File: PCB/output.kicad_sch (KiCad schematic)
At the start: 8 parts, among them J2 Output Gate, Q1 BC547

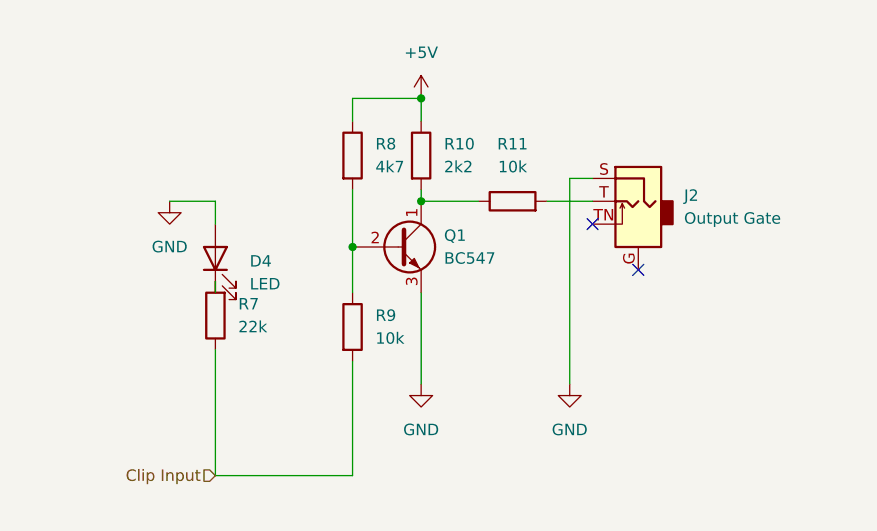
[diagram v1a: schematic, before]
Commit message: :art: Adjust layout of Clip CV input
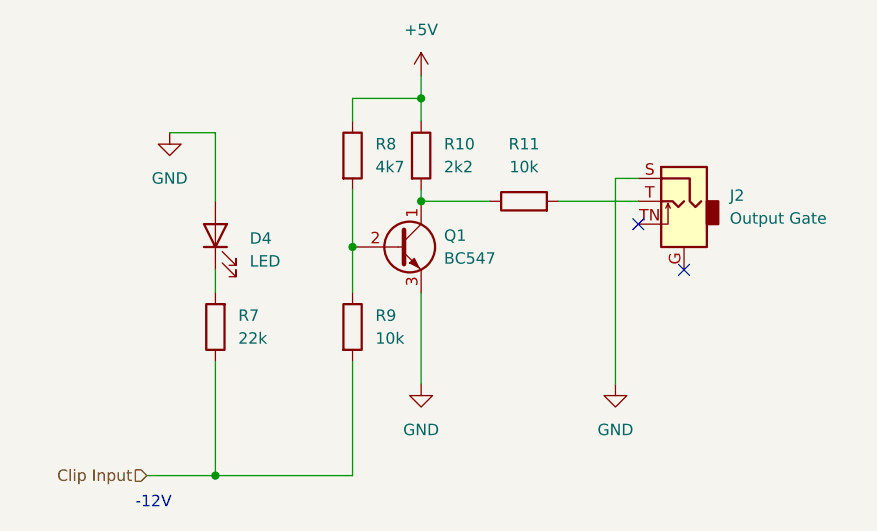
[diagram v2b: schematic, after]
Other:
- note added: "-12V"
- moved on the sheet: D4, J2, R11, R7

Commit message: :wrench: Re-assign component designators
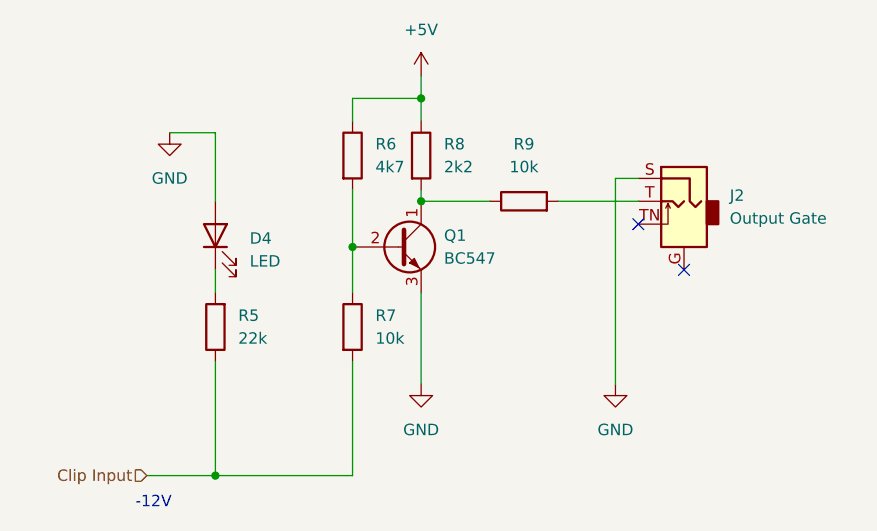
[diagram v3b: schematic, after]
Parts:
- renumbered R7 to R5, R8 to R6, R9 to R7, R10 to R8, R11 to R9
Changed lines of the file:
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@@
   (symbol (lib_id "Device:R") (at 137.16 96.52 180) (unit 1)
     (in_bom yes) (on_board yes) (dnp no) (fields_autoplaced)
-    (property "Reference" "R7" (at 139.7 95.2499 0)
+    (property "Reference" "R5" (at 139.7 95.2499 0)
       (effects (font (size 1.27 1.27)) (justify right))
     )
@@
       (project "misterclippy"
         (path "/e63e39d7-6ac0-4ffd-8aa3-1841a4541b55/28e15989-5385-427e-a9a7-25fddc57d8c9"
-          (reference "R7") (unit 1)
-        )
-        (path "/e63e39d7-6ac0-4ffd-8aa3-1841a4541b55/cb5a0e2d-897e-4b15-92a1-7875a38841f1"
-          (reference "R12") (unit 1)
+          (reference "R5") (unit 1)
+        )
+        (path "/e63e39d7-6ac0-4ffd-8aa3-1841a4541b55/cb5a0e2d-897e-4b15-92a1-7875a38841f1"
+          (reference "R10") (unit 1)
         )
       )
@@
   (symbol (lib_id "power:GND") (at 132.08 74.93 0) (unit 1)
     (in_bom yes) (on_board yes) (dnp no) (fields_autoplaced)
-    (property "Reference" "#PWR0120" (at 132.08 81.28 0)
+    (property "Reference" "#PWR015" (at 132.08 81.28 0)
       (effects (font (size 1.27 1.27)) hide)
     )
@@
       (project "misterclippy"
         (path "/e63e39d7-6ac0-4ffd-8aa3-1841a4541b55/28e15989-5385-427e-a9a7-25fddc57d8c9"
-          (reference "#PWR0120") (unit 1)
-        )
-        (path "/e63e39d7-6ac0-4ffd-8aa3-1841a4541b55/cb5a0e2d-897e-4b15-92a1-7875a38841f1"
-          (reference "#PWR0124") (unit 1)
+          (reference "#PWR015") (unit 1)
+        )
+        (path "/e63e39d7-6ac0-4ffd-8aa3-1841a4541b55/cb5a0e2d-897e-4b15-92a1-7875a38841f1"
+          (reference "#PWR019") (unit 1)
         )
       )
@@
   (symbol (lib_id "power:GND") (at 181.61 102.87 0) (unit 1)
     (in_bom yes) (on_board yes) (dnp no) (fields_autoplaced)
-    (property "Reference" "#PWR0118" (at 181.61 109.22 0)
+    (property "Reference" "#PWR018" (at 181.61 109.22 0)
       (effects (font (size 1.27 1.27)) hide)
     )
@@
       (project "misterclippy"
         (path "/e63e39d7-6ac0-4ffd-8aa3-1841a4541b55/28e15989-5385-427e-a9a7-25fddc57d8c9"
-          (reference "#PWR0118") (unit 1)
-        )
-        (path "/e63e39d7-6ac0-4ffd-8aa3-1841a4541b55/cb5a0e2d-897e-4b15-92a1-7875a38841f1"
-          (reference "#PWR0122") (unit 1)
+          (reference "#PWR018") (unit 1)
+        )
+        (path "/e63e39d7-6ac0-4ffd-8aa3-1841a4541b55/cb5a0e2d-897e-4b15-92a1-7875a38841f1"
+          (reference "#PWR022") (unit 1)
         )
       )
@@
   (symbol (lib_id "power:+5V") (at 160.02 68.58 0) (unit 1)
     (in_bom yes) (on_board yes) (dnp no) (fields_autoplaced)
-    (property "Reference" "#PWR0117" (at 160.02 72.39 0)
+    (property "Reference" "#PWR016" (at 160.02 72.39 0)
       (effects (font (size 1.27 1.27)) hide)
     )
@@
       (project "misterclippy"
         (path "/e63e39d7-6ac0-4ffd-8aa3-1841a4541b55/28e15989-5385-427e-a9a7-25fddc57d8c9"
-          (reference "#PWR0117") (unit 1)
-        )
-        (path "/e63e39d7-6ac0-4ffd-8aa3-1841a4541b55/cb5a0e2d-897e-4b15-92a1-7875a38841f1"
-          (reference "#PWR0121") (unit 1)
+          (reference "#PWR016") (unit 1)
+        )
+        (path "/e63e39d7-6ac0-4ffd-8aa3-1841a4541b55/cb5a0e2d-897e-4b15-92a1-7875a38841f1"
+          (reference "#PWR020") (unit 1)
         )
       )
@@
   (symbol (lib_id "Device:R") (at 160.02 77.47 0) (unit 1)
     (in_bom yes) (on_board yes) (dnp no) (fields_autoplaced)
-    (property "Reference" "R10" (at 162.56 76.1999 0)
+    (property "Reference" "R8" (at 162.56 76.1999 0)
       (effects (font (size 1.27 1.27)) (justify left))
     )
@@
       (project "misterclippy"
         (path "/e63e39d7-6ac0-4ffd-8aa3-1841a4541b55/28e15989-5385-427e-a9a7-25fddc57d8c9"
-          (reference "R10") (unit 1)
-        )
-        (path "/e63e39d7-6ac0-4ffd-8aa3-1841a4541b55/cb5a0e2d-897e-4b15-92a1-7875a38841f1"
-          (reference "R15") (unit 1)
+          (reference "R8") (unit 1)
+        )
+        (path "/e63e39d7-6ac0-4ffd-8aa3-1841a4541b55/cb5a0e2d-897e-4b15-92a1-7875a38841f1"
+          (reference "R13") (unit 1)
         )
       )
@@
   (symbol (lib_id "Device:R") (at 152.4 96.52 0) (unit 1)
     (in_bom yes) (on_board yes) (dnp no) (fields_autoplaced)
-    (property "Reference" "R9" (at 154.94 95.2499 0)
+    (property "Reference" "R7" (at 154.94 95.2499 0)
       (effects (font (size 1.27 1.27)) (justify left))
     )
@@
       (project "misterclippy"
         (path "/e63e39d7-6ac0-4ffd-8aa3-1841a4541b55/28e15989-5385-427e-a9a7-25fddc57d8c9"
+          (reference "R7") (unit 1)
+        )
+        (path "/e63e39d7-6ac0-4ffd-8aa3-1841a4541b55/cb5a0e2d-897e-4b15-92a1-7875a38841f1"
+          (reference "R12") (unit 1)
+        )
+      )
+    )
+  )
+  (symbol (lib_id "Device:R") (at 152.4 77.47 0) (unit 1)
+    (in_bom yes) (on_board yes) (dnp no) (fields_autoplaced)
+    (property "Reference" "R6" (at 154.94 76.1999 0)
+      (effects (font (size 1.27 1.27)) (justify left))
+    )
+    (property "Value" "4k7" (at 154.94 78.7399 0)
+      (effects (font (size 1.27 1.27)) (justify left))
+    )
+    (property "Footprint" "Resistor_THT:R_Axial_DIN0207_L6.3mm_D2.5mm_P7.62mm_Horizontal" (at 150.622 77.47 90)
+      (effects (font (size 1.27 1.27)) hide)
+    )
+    (property "Datasheet" "~" (at 152.4 77.47 0)
+      (effects (font (size 1.27 1.27)) hide)
+    )
+    (pin "1")
+    (pin "2")
+    (instances
+      (project "misterclippy"
+        (path "/e63e39d7-6ac0-4ffd-8aa3-1841a4541b55/28e15989-5385-427e-a9a7-25fddc57d8c9"
+          (reference "R6") (unit 1)
+        )
+        (path "/e63e39d7-6ac0-4ffd-8aa3-1841a4541b55/cb5a0e2d-897e-4b15-92a1-7875a38841f1"
+          (reference "R11") (unit 1)
+        )
+      )
+    )
+  )
+  (symbol (lib_id "Device:R") (at 171.45 82.55 90) (unit 1)
+    (in_bom yes) (on_board yes) (dnp no) (fields_autoplaced)
+    (property "Reference" "R9" (at 171.45 76.2 90)
+      (effects (font (size 1.27 1.27)))
+    )
+    (property "Value" "10k" (at 171.45 78.74 90)
+      (effects (font (size 1.27 1.27)))
+    )
+    (property "Footprint" "Resistor_THT:R_Axial_DIN0207_L6.3mm_D2.5mm_P7.62mm_Horizontal" (at 171.45 84.328 90)
+      (effects (font (size 1.27 1.27)) hide)
+    )
+    (property "Datasheet" "~" (at 171.45 82.55 0)
+      (effects (font (size 1.27 1.27)) hide)
+    )
+    (pin "1")
+    (pin "2")
+    (instances
+      (project "misterclippy"
+        (path "/e63e39d7-6ac0-4ffd-8aa3-1841a4541b55/28e15989-5385-427e-a9a7-25fddc57d8c9"
           (reference "R9") (unit 1)
         )
         (path "/e63e39d7-6ac0-4ffd-8aa3-1841a4541b55/cb5a0e2d-897e-4b15-92a1-7875a38841f1"
           (reference "R14") (unit 1)
-        )
-      )
-    )
-  )
-  (symbol (lib_id "Device:R") (at 152.4 77.47 0) (unit 1)
-    (in_bom yes) (on_board yes) (dnp no) (fields_autoplaced)
-    (property "Reference" "R8" (at 154.94 76.1999 0)
-      (effects (font (size 1.27 1.27)) (justify left))
-    )
-    (property "Value" "4k7" (at 154.94 78.7399 0)
-      (effects (font (size 1.27 1.27)) (justify left))
-    )
-    (property "Footprint" "Resistor_THT:R_Axial_DIN0207_L6.3mm_D2.5mm_P7.62mm_Horizontal" (at 150.622 77.47 90)
-      (effects (font (size 1.27 1.27)) hide)
-    )
-    (property "Datasheet" "~" (at 152.4 77.47 0)
-      (effects (font (size 1.27 1.27)) hide)
-    )
-    (pin "1")
-    (pin "2")
-    (instances
-      (project "misterclippy"
-        (path "/e63e39d7-6ac0-4ffd-8aa3-1841a4541b55/28e15989-5385-427e-a9a7-25fddc57d8c9"
-          (reference "R8") (unit 1)
-        )
-        (path "/e63e39d7-6ac0-4ffd-8aa3-1841a4541b55/cb5a0e2d-897e-4b15-92a1-7875a38841f1"
-          (reference "R13") (unit 1)
-        )
-      )
-    )
-  )
-  (symbol (lib_id "Device:R") (at 171.45 82.55 90) (unit 1)
-    (in_bom yes) (on_board yes) (dnp no) (fields_autoplaced)
-    (property "Reference" "R11" (at 171.45 76.2 90)
-      (effects (font (size 1.27 1.27)))
-    )
-    (property "Value" "10k" (at 171.45 78.74 90)
-      (effects (font (size 1.27 1.27)))
-    )
-    (property "Footprint" "Resistor_THT:R_Axial_DIN0207_L6.3mm_D2.5mm_P7.62mm_Horizontal" (at 171.45 84.328 90)
-      (effects (font (size 1.27 1.27)) hide)
-    )
-    (property "Datasheet" "~" (at 171.45 82.55 0)
-      (effects (font (size 1.27 1.27)) hide)
-    )
-    (pin "1")
-    (pin "2")
-    (instances
-      (project "misterclippy"
-        (path "/e63e39d7-6ac0-4ffd-8aa3-1841a4541b55/28e15989-5385-427e-a9a7-25fddc57d8c9"
-          (reference "R11") (unit 1)
-        )
-        (path "/e63e39d7-6ac0-4ffd-8aa3-1841a4541b55/cb5a0e2d-897e-4b15-92a1-7875a38841f1"
-          (reference "R16") (unit 1)
         )
       )
@@
   (symbol (lib_id "power:GND") (at 160.02 102.87 0) (unit 1)
     (in_bom yes) (on_board yes) (dnp no) (fields_autoplaced)
-    (property "Reference" "#PWR0119" (at 160.02 109.22 0)
+    (property "Reference" "#PWR017" (at 160.02 109.22 0)
       (effects (font (size 1.27 1.27)) hide)
     )
@@
       (project "misterclippy"
         (path "/e63e39d7-6ac0-4ffd-8aa3-1841a4541b55/28e15989-5385-427e-a9a7-25fddc57d8c9"
-          (reference "#PWR0119") (unit 1)
-        )
-        (path "/e63e39d7-6ac0-4ffd-8aa3-1841a4541b55/cb5a0e2d-897e-4b15-92a1-7875a38841f1"
-          (reference "#PWR0123") (unit 1)
-        )
-      )
+          (reference "#PWR017") (unit 1)
+        )
+        (path "/e63e39d7-6ac0-4ffd-8aa3-1841a4541b55/cb5a0e2d-897e-4b15-92a1-7875a38841f1"
+          (reference "#PWR021") (unit 1)
+        )
+      )

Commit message: :wrench: Replace audio jack footprints by centered versions
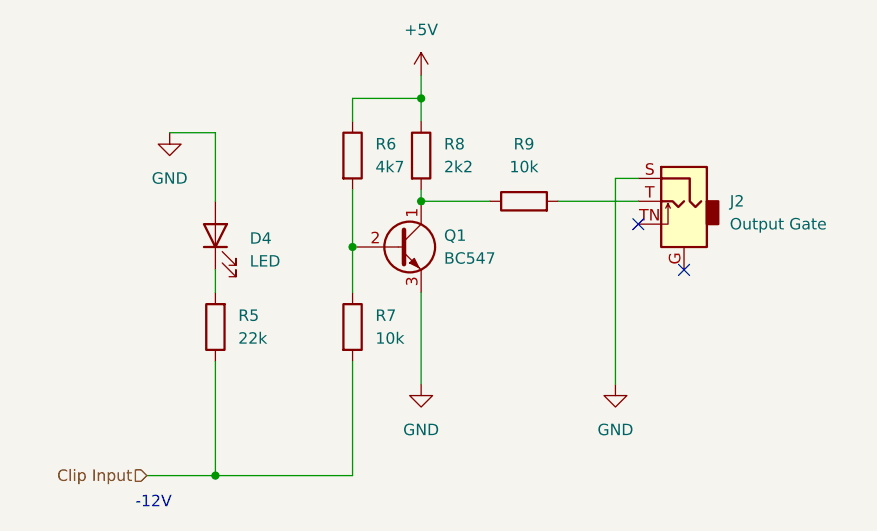
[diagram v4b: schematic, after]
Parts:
- J2: footprint Connector_Audio:Jack_3.5mm_QingPu_WQP-PJ398SM_Vertical_CircularHoles -> mopsy:Jack_3.5mm_QingPu_WQP-PJ398SM_Vertical_CircularHoles_Centered
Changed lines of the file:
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@@
   (symbol (lib_id "Connector:AudioJack2_Ground_SwitchT") (at 189.23 82.55 0) (mirror y) (unit 1)
     (in_bom yes) (on_board yes) (dnp no) (fields_autoplaced)
-    (property "Reference" "J2" (at 194.31 81.9149 0)
+    (property "Reference" "J2" (at 194.31 82.55 0)
       (effects (font (size 1.27 1.27)) (justify right))
     )
-    (property "Value" "Output Gate" (at 194.31 84.4549 0)
+    (property "Value" "Output Gate" (at 194.31 85.09 0)
       (effects (font (size 1.27 1.27)) (justify right))
     )
-    (property "Footprint" "Connector_Audio:Jack_3.5mm_QingPu_WQP-PJ398SM_Vertical_CircularHoles" (at 189.23 82.55 0)
+    (property "Footprint" "mopsy:Jack_3.5mm_QingPu_WQP-PJ398SM_Vertical_CircularHoles_Centered" (at 189.23 82.55 0)
       (effects (font (size 1.27 1.27)) hide)
     )

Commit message: fix schematics after further testing
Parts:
- R7: value 10k -> 4k7
- R9: value 10k -> 1k
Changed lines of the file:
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@@
   (symbol (lib_id "Device:R") (at 152.4 96.52 0) (unit 1)
     (in_bom yes) (on_board yes) (dnp no) (fields_autoplaced)
-    (property "Reference" "R7" (at 154.94 95.2499 0)
+    (property "Reference" "R7" (at 154.94 95.885 0)
       (effects (font (size 1.27 1.27)) (justify left))
     )
-    (property "Value" "10k" (at 154.94 97.7899 0)
+    (property "Value" "4k7" (at 154.94 98.425 0)
       (effects (font (size 1.27 1.27)) (justify left))
     )
@@
   (symbol (lib_id "Device:R") (at 171.45 82.55 90) (unit 1)
     (in_bom yes) (on_board yes) (dnp no) (fields_autoplaced)
-    (property "Reference" "R9" (at 171.45 76.2 90)
+    (property "Reference" "R9" (at 171.45 77.47 90)
       (effects (font (size 1.27 1.27)))
     )
-    (property "Value" "10k" (at 171.45 78.74 90)
+    (property "Value" "1k" (at 171.45 80.01 90)
       (effects (font (size 1.27 1.27)))
     )
